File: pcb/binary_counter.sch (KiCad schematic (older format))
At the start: 55 parts, among them IC1 ATXMEGA256A3BU-A, J1 DB9M, J2 DB9F, J3 DB9F, P1 CONN_01X02, P10 CONN_01X03, P11 CONN_01X05, P12 CONN_01X06, P13 CONN_01X03, P2 CONN_01X02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

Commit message: started revising schematic and specifying components.
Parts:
- removed BT1, BT2, BT3, BT4: 1.5V AA LITHIUM, symbol imu_daq_hardware-rescue:Battery
- removed C10, C7, C8, C9: 0.1uF, symbol imu_daq_hardware-rescue:CP
- removed C11, C13, C14, C2: 0.1uF, symbol imu_daq_hardware-rescue:C
- removed C4: 10uF, symbol imu_daq_hardware-rescue:CP
- removed D1, D2: LED, symbol imu_daq_hardware-rescue:LED
- removed J1: DB9M, symbol imu_daq_hardware-rescue:DB9
- removed J2, J3: DB9F, symbol imu_daq_hardware-rescue:DB9
- removed P1, P2, P3, P4, P5, P6: CONN_01X02, symbol imu_daq_hardware-rescue:CONN_01X02
- removed P11, P8: CONN_01X05, symbol imu_daq_hardware-rescue:CONN_01X05
- removed P12, P9: CONN_01X06, symbol imu_daq_hardware-rescue:CONN_01X06
- removed P13: CONN_01X03, symbol imu_daq_hardware-rescue:CONN_01X03
- removed R1: 68R, symbol imu_daq_hardware-rescue:R
- removed R10, R9: 33K, symbol imu_daq_hardware-rescue:R
- removed R11: 180R, symbol imu_daq_hardware-rescue:R
- removed R3, R4, R5, R6: 33R, symbol imu_daq_hardware-rescue:R
- removed R7, R8: 56K, symbol imu_daq_hardware-rescue:R
- removed SW1: SPST, symbol imu_daq_hardware-rescue:SPST
- removed U1: LM1086CT-3.3/NOPB, TO-220, symbol imu_daq_hardware-rescue:LM1084IT-3.3_NOPB
- removed U2: 7805, symbol imu_daq_hardware-rescue:7805
- removed U3: MAX3221, symbol imu_daq_hardware-rescue:MAX3221
- removed U4: LS7166, symbol imu_daq_hardware-rescue:LS7166
- removed U5: STEVAL-MKI160V1, symbol imu_daq_hardware-rescue:STEVAL-MKI160V1
- added D1, D2, D3, D4, D5, D6, D7, D8: LTST-C150KRKT, digikey-footprints:1206, symbol dk_LED-Indication-Discrete:LTST-C150KRKT
- added J1: Conn_01x02_Male, symbol Connector:Conn_01x02_Male
- added R2, R3, R4, R5, R6, R7, R8, R9: 50R, symbol Device:R
- added TP1: TestPoint, symbol Connector:TestPoint
- C4: renamed from C5; value 18pF -> 3pF
- C5: renamed from C6; value 18pF -> 3pF
- renumbered C12 to C1, C1 to C2, P7 to J2, P10 to J3, R2 to R1
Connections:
- net RXD is gone; now on an unnamed net: J3.3 (P3)
- net TXD is gone; now on an unnamed net: J3.2 (P2)
- net +3V3: no longer C2.1, C3.1, R1.2
- net GND: now also J1.2 (Pin_2)
- net at IC1.10 (TMS/AC4/ADC4/ADC12/PB4): now also R6.2
- net at IC1.11 (TDI/AC5/ADC5/ADC13/PB5): now also R7.2
- net at IC1.12 (TCK/AC1OUT/AC6/ADC6/ADC14/PB6): now also R8.2
- net at IC1.13 (TDO/AC0OUT/AC7/ADC7/ADC15/PB7): now also R9.2
- net at IC1.6 (AREF/AC0/ADC0/ADC8/PB0): now also R2.2
- net at IC1.62 (AREF/AC0/ADC8/ADC0/PA0): now also TP1.1
- net at IC1.7 (AC1/ADC1/ADC9/PB1): now also R3.2
- net at IC1.8 (DAC0/AC2/ADC2/ADC10/PB2): now also R4.2
- net at IC1.9 (DAC1/AC3/ADC3/ADC11/PB3): now also R5.2
- new net: D1.2, R2.1
- new net: D2.2, R3.1
- new net: D3.2, R4.1
- new net: D4.2, R5.1
- new net: D5.2, R6.1
- new net: D6.2, R7.1
- new net: D7.2, R8.1
- new net: D8.2, R9.1
- new net +3V0: C2.1, C3.1, D1.1, D2.1, D3.1, D4.1, D5.1, D6.1, D7.1, D8.1, J1.1 (Pin_1), R1.2
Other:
- note removed: "2X KEYSTONE\n2463 OR SIMILAR\nDOBULE AA \nBATTERY HOLDER"
- note removed: "BREADBOARD"
- note removed: "E-SWITCH\nRR3130ABLKBLKFS\nOR SIMILAR"
- note removed: "KEYBOARD CABLE TRIPP-LITE P222-015 OR SIMILAR"
- note removed: "LUMEX\nSSI-LXH600GD-150\nOR SIMILAR"
- note removed: "NOTE: +5VDC BUS\nREQUIRED ONLY IF\nOPTICAL ENCODER\nINTERFACE PRESENT"
- note removed: "NOTE: A & B CHANNELS NOT\nBUFFERED. US DIGITAL E6\nENCODER OUTPUT RATED TO\n±8mA; MAX LS7166 LEAKAGE\n15nA. NOMINAL CURRENT IN\nVOLTAGE DIVIDER SET TO 56μA"
- note removed: "NOTE: POPULATE LS7166\nAND CONNECTOR ONLY\nON IMU CALIBRATION\nINTERFACE BOARD"
- note removed: "OPTICAL ENCODER CONNECTION\nFOR CALIBRATION / ALIGNMENT\nUS DIGITAL PART #CA-FC5-SH-FC5-4"
- note removed: "PROTOTYPE VERASENSE TRIAL\nWITH ST #LSM6DS3 INERTIAL MEASUREMENT UNIT"
- note removed: "RS232 DATA\nCONNECTION"
- moved on the sheet: C2, C3, J3

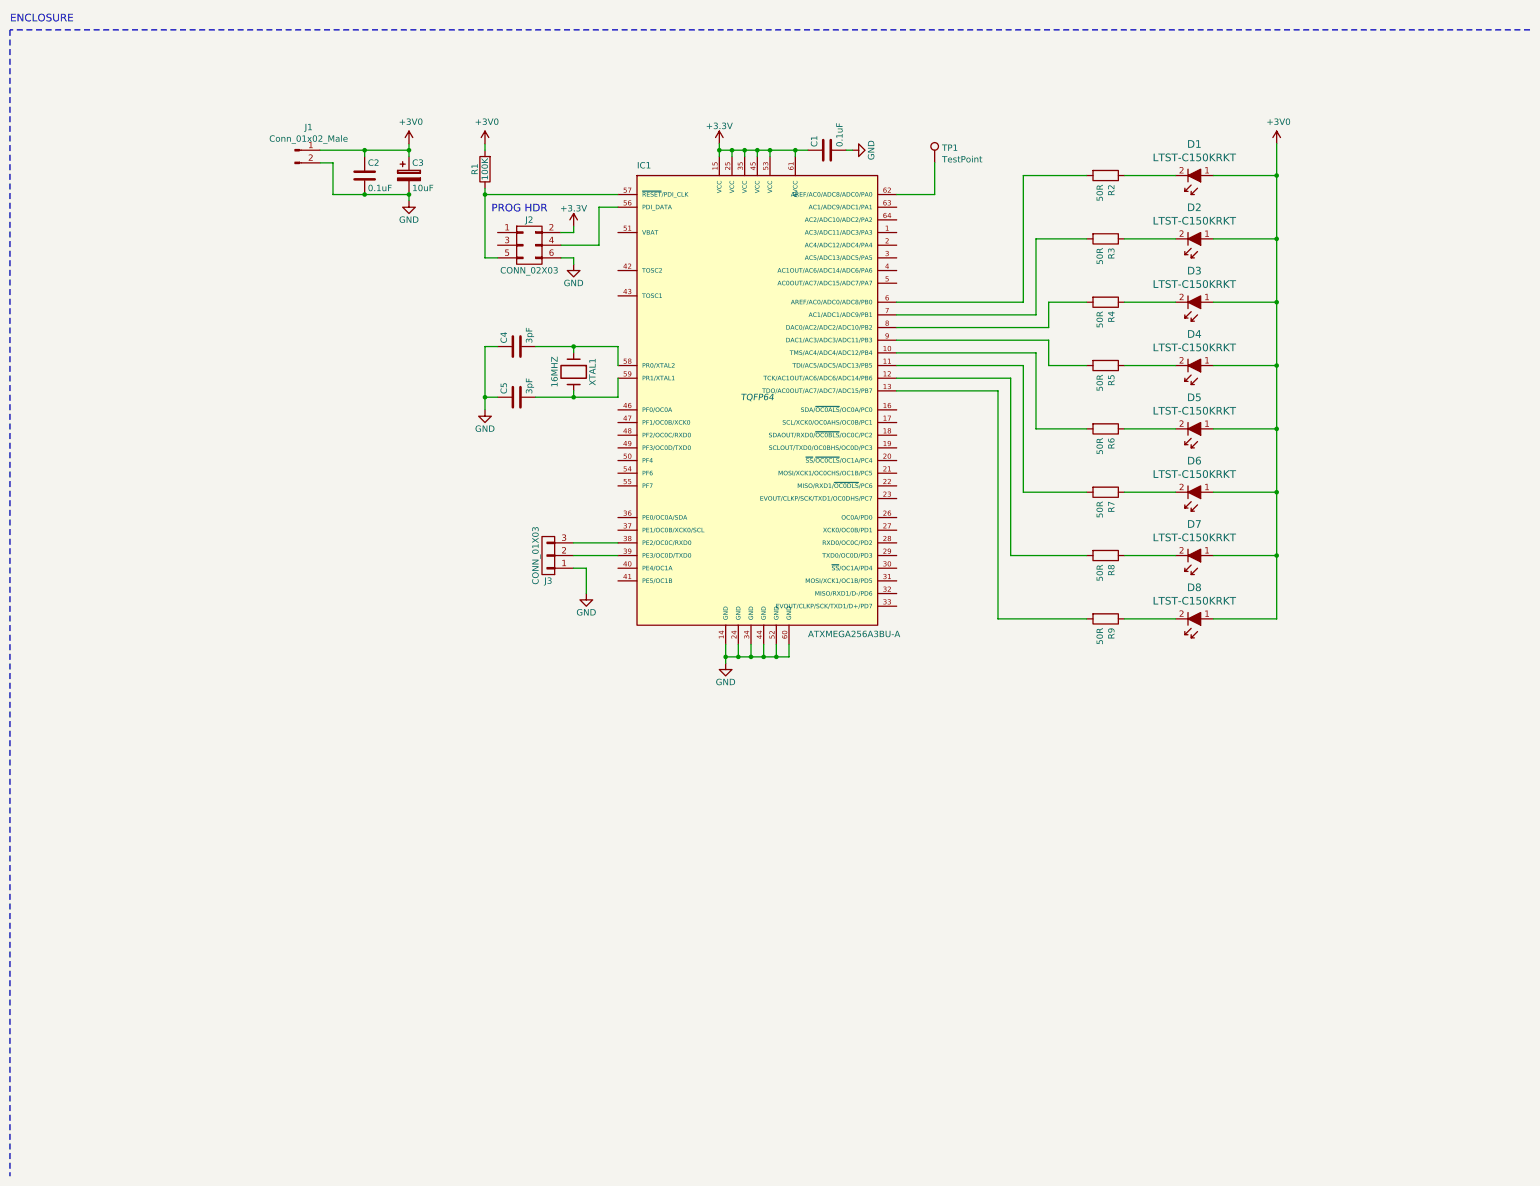
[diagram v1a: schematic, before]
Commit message: continued adding footprints, etc.
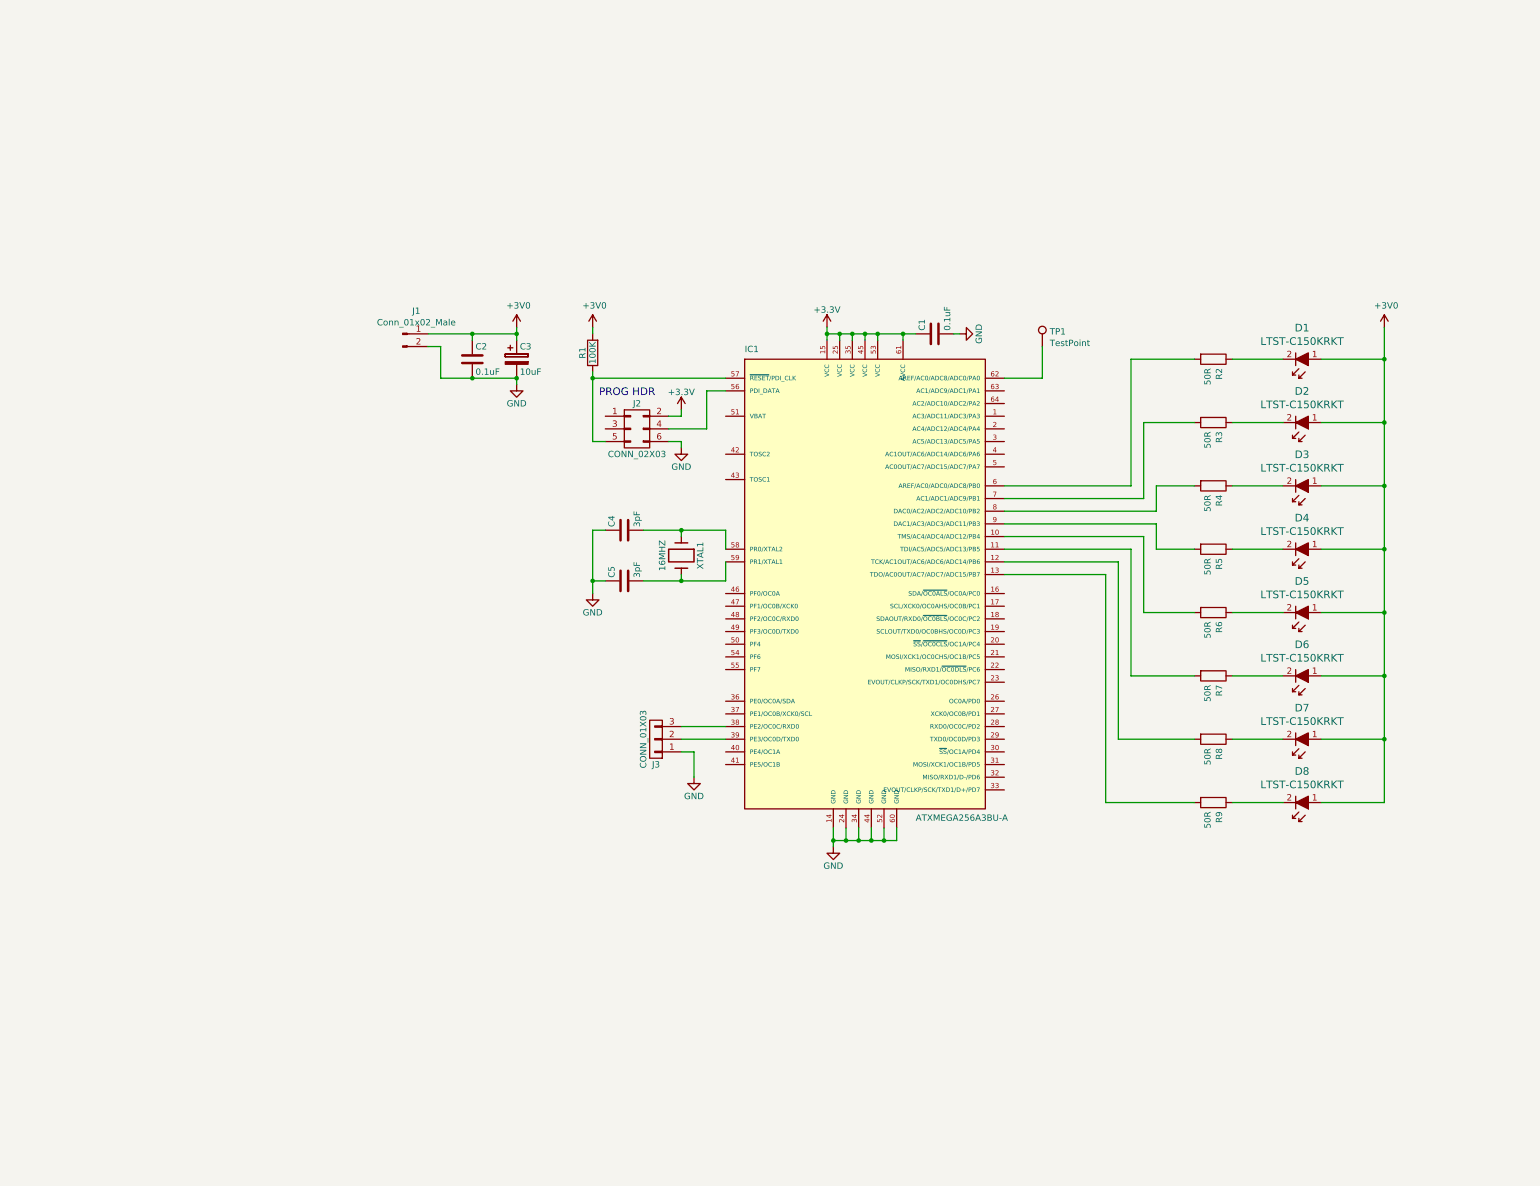
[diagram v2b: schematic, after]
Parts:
- C1, C2, C3, C4, C5, R1, R2, R3, R4, R5, R6, R7, R8, R9: footprint (none) -> digikey-footprints:1206
- IC1: footprint TQFP64 -> Package_QFP:TQFP-64_14x14mm_P0.8mm
- J2: footprint (none) -> binary_counter_footprints:prog_header
- XTAL1: footprint (none) -> binary_counter_footprints:TXC_xtal
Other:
- note removed: "ENCLOSURE"
- moved on the sheet: C1, C2, C3, C4, C5, D1, D2, D3, D4, D5, D6, D7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

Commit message: finished adding footprints and started laying out board
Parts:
- added SW1: SW_SPDT, binary_counter_footprints:SWITCH_CK_JS102011SAQN, symbol Switch:SW_SPDT
- J1: footprint (none) -> binary_counter_footprints:Molex_15_91_2025
- J3: footprint (none) -> binary_counter_footprints:Molex_15_91_2035
- R2, R3, R4, R5, R6, R7, R8, R9: value 50R -> 47R0
- TP1: footprint (none) -> TestPoint:TestPoint_Pad_D1.5mm
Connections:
- net +3V0: now also SW1.3 (C); no longer J1.1 (Pin_1)
- new net: J1.1 (Pin_1), SW1.2 (B)
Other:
- moved on the sheet: J1
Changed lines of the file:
@@
 Wire Wire Line
 	4650 3200 4650 3250
-Connection ~ 4300 3250
 Wire Wire Line
 	7100 3200 7100 3250
@@
 P 10150 3450
 F 0 "R2" H 10220 3496 50  0000 L CNN
-F 1 "50R" H 10220 3405 50  0000 L CNN
+F 1 "47R0" H 10220 3405 50  0000 L CNN
 F 2 "digikey-footprints:1206" V 10080 3450 50  0001 C CNN
 F 3 "~" H 10150 3450 50  0001 C CNN
@@
 F 0 "J3" H 5750 6650 50  0000 C CNN
 F 1 "CONN_01X03" V 5850 6450 50  0000 C CNN
-F 2 "" H 5750 6450 50  0001 C CNN
+F 2 "binary_counter_footprints:Molex_15_91_2035" H 5750 6450 50  0001 C CNN
 F 3 "" H 5750 6450 50  0000 C CNN
 	1    5750 6450
@@
 	1    0    0    -1
 $EndComp
-Wire Wire Line
-	4050 3600 4300 3600
-Wire Wire Line
-	4050 3600 4050 3350
-Wire Wire Line
-	3950 3350 4050 3350
-Wire Wire Line
-	3950 3250 4300 3250
 $Comp
 L Connector:Conn_01x02_Male J1
 U 1 1 5D14429C
-P 3750 3250
-F 0 "J1" H 3858 3431 50  0000 C CNN
-F 1 "Conn_01x02_Male" H 3858 3340 50  0000 C CNN
-F 2 "" H 3750 3250 50  0001 C CNN
-F 3 "~" H 3750 3250 50  0001 C CNN
-	1    3750 3250
+P 3100 3350
+F 0 "J1" H 3208 3531 50  0000 C CNN
+F 1 "Conn_01x02_Male" H 3208 3440 50  0000 C CNN
+F 2 "binary_counter_footprints:Molex_15_91_2025" H 3100 3350 50  0001 C CNN
+F 3 "~" H 3100 3350 50  0001 C CNN
+	1    3100 3350
 	1    0    0    -1
 $EndComp
@@
 P 10150 3950
 F 0 "R3" H 10220 3996 50  0000 L CNN
-F 1 "50R" H 10220 3905 50  0000 L CNN
+F 1 "47R0" H 10220 3905 50  0000 L CNN
 F 2 "digikey-footprints:1206" V 10080 3950 50  0001 C CNN
 F 3 "~" H 10150 3950 50  0001 C CNN
@@
 P 10150 4450
 F 0 "R4" H 10220 4496 50  0000 L CNN
-F 1 "50R" H 10220 4405 50  0000 L CNN
+F 1 "47R0" H 10220 4405 50  0000 L CNN
 F 2 "digikey-footprints:1206" V 10080 4450 50  0001 C CNN
 F 3 "~" H 10150 4450 50  0001 C CNN
@@
 P 10150 4950
 F 0 "R5" H 10220 4996 50  0000 L CNN
-F 1 "50R" H 10220 4905 50  0000 L CNN
+F 1 "47R0" H 10220 4905 50  0000 L CNN
 F 2 "digikey-footprints:1206" V 10080 4950 50  0001 C CNN
 F 3 "~" H 10150 4950 50  0001 C CNN
@@
 P 10150 5450
 F 0 "R6" H 10220 5496 50  0000 L CNN
-F 1 "50R" H 10220 5405 50  0000 L CNN
+F 1 "47R0" H 10220 5405 50  0000 L CNN
 F 2 "digikey-footprints:1206" V 10080 5450 50  0001 C CNN
 F 3 "~" H 10150 5450 50  0001 C CNN
@@
 P 10150 5950
 F 0 "R7" H 10220 5996 50  0000 L CNN
-F 1 "50R" H 10220 5905 50  0000 L CNN
+F 1 "47R0" H 10220 5905 50  0000 L CNN
 F 2 "digikey-footprints:1206" V 10080 5950 50  0001 C CNN
 F 3 "~" H 10150 5950 50  0001 C CNN
@@
 P 10150 6450
 F 0 "R8" H 10220 6496 50  0000 L CNN
-F 1 "50R" H 10220 6405 50  0000 L CNN
+F 1 "47R0" H 10220 6405 50  0000 L CNN
 F 2 "digikey-footprints:1206" V 10080 6450 50  0001 C CNN
 F 3 "~" H 10150 6450 50  0001 C CNN
@@
 P 10150 6950
 F 0 "R9" H 10220 6996 50  0000 L CNN
-F 1 "50R" H 10220 6905 50  0000 L CNN
+F 1 "47R0" H 10220 6905 50  0000 L CNN
 F 2 "digikey-footprints:1206" V 10080 6950 50  0001 C CNN
 F 3 "~" H 10150 6950 50  0001 C CNN
@@
 F 0 "TP1" H 8858 3468 50  0000 L CNN
 F 1 "TestPoint" H 8858 3377 50  0000 L CNN
-F 2 "" H 9000 3350 50  0001 C CNN
+F 2 "TestPoint:TestPoint_Pad_D1.5mm" H 9000 3350 50  0001 C CNN
 F 3 "~" H 9000 3350 50  0001 C CNN
 	1    8800 3350
@@
 Wire Wire Line
 	5950 6350 6300 6350
+$Comp
+L Switch:SW_SPDT SW1
+U 1 1 5D096841
+P 3800 3350
+F 0 "SW1" H 3800 3635 50  0000 C CNN
+F 1 "SW_SPDT" H 3800 3544 50  0000 C CNN
+F 2 "binary_counter_footprints:SWITCH_CK_JS102011SAQN" H 3800 3350 50  0001 C CNN
+F 3 "~" H 3800 3350 50  0001 C CNN
+	1    3800 3350
+	1    0    0    -1
+$EndComp
+Wire Wire Line
+	3300 3350 3600 3350
+Wire Wire Line
+	3300 3450 3500 3450
+Wire Wire Line
+	3500 3450 3500 3600
+Wire Wire Line
+	3500 3600 4300 3600
+Wire Wire Line
+	4000 3450 4100 3450
+Wire Wire Line
+	4100 3450 4100 3250
+Wire Wire Line
+	4100 3250 4300 3250
+Connection ~ 4300 3250
 $EndSCHEMATC
